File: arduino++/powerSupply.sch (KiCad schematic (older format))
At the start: 10 parts, among them U2 NCP551SN33T1G, U8 LD1085C

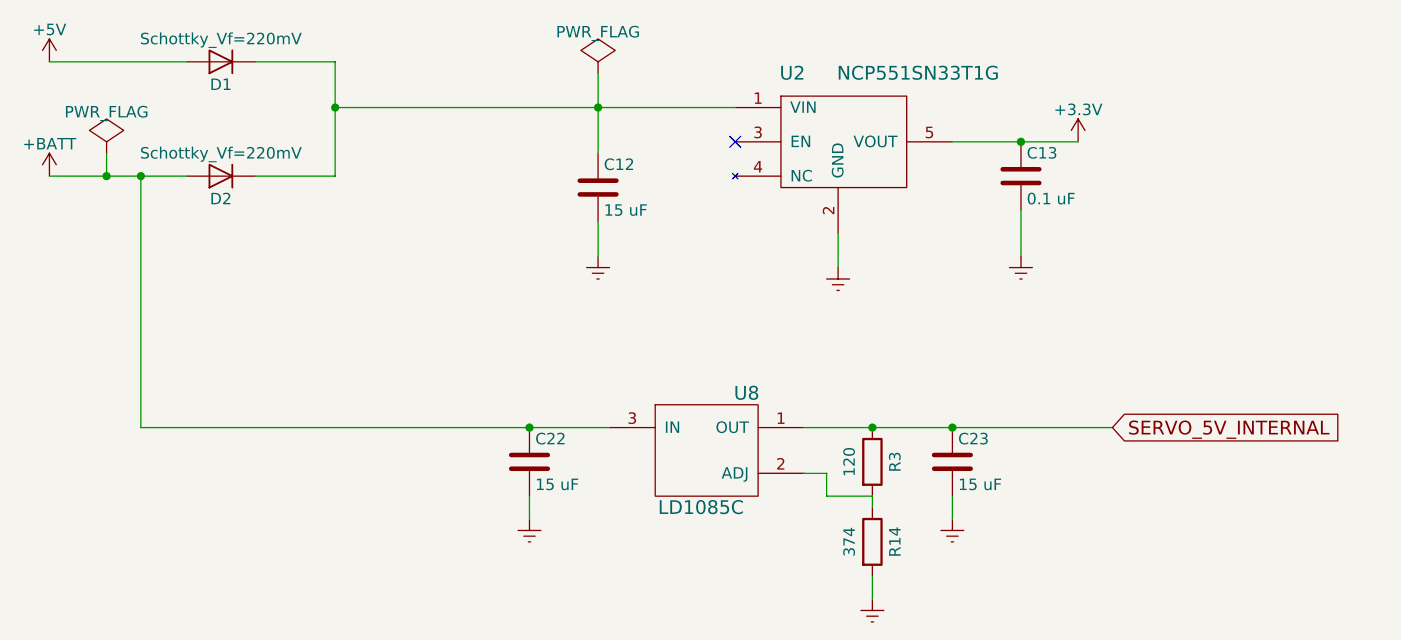
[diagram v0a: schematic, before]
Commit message: Updating to latest rev as ordered on OSHPark.
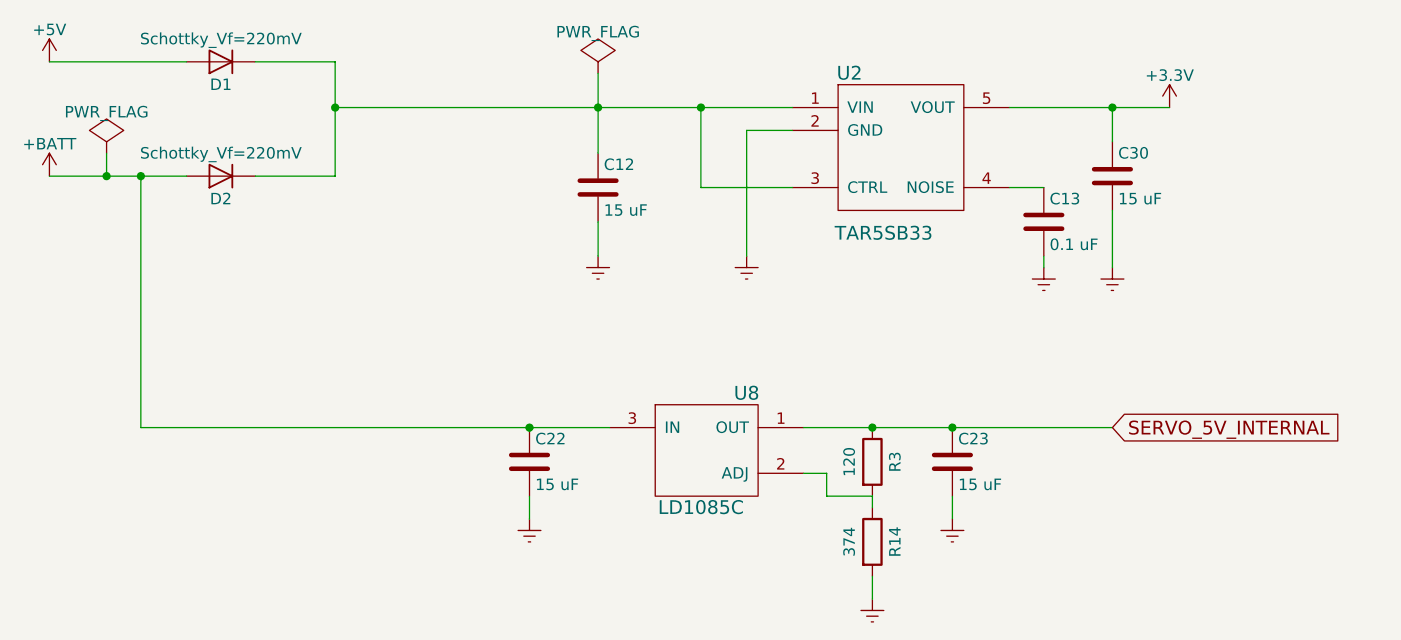
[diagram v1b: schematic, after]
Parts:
- removed U2: NCP551SN33T1G, Housings_SOT-23_SOT-143_TSOT-6:SOT-23-5, symbol NCP551SN33T1G
- added C30: 15 uF, Capacitors_SMD:C_0805_HandSoldering, symbol C
- added U2: TAR5SB33, housings_sot_custom:SC-74A_SOT23-5, symbol TAR5SB33
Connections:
- net +3V3: now also C30.1, U2.5 (VOUT); no longer C13.1
- net Earth: now also C30.2, U2.2 (GND)
- net at C12.1, D1.1 (K), D2.1 (K): now also U2.1 (VIN), U2.3 (CTRL)
- new net: C13.1, U2.4 (NOISE)
- no-connect marks 1 -> 0
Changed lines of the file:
@@
 	4350 3650 4000 3650
 $Comp
-L +5V #PWR054
+L +5V #PWR52
 U 1 1 5834CD49
 P 3100 3150
-F 0 "#PWR054" H 3100 3000 50  0001 C CNN
+F 0 "#PWR52" H 3100 3000 50  0001 C CNN
 F 1 "+5V" H 3100 3290 50  0000 C CNN
 F 2 "" H 3100 3150 50  0000 C CNN
@@
 $EndComp
 Wire Wire Line
-	4350 3350 6100 3350
+	4350 3350 6350 3350
 Connection ~ 4350 3350
 $Comp
-L NCP551SN33T1G U2
-U 1 1 5834E7B3
-P 6600 3500
-F 0 "U2" H 6350 3800 60  0000 C CNN
-F 1 "NCP551SN33T1G" H 6900 3800 60  0000 C CNN
-F 2 "Housings_SOT-23_SOT-143_TSOT-6:SOT-23-5" H 6600 3500 60  0001 C CNN
-F 3 "" H 6600 3500 60  0001 C CNN
-	1    6600 3500
-	1    0    0    -1
-$EndComp
-$Comp
-L Earth #PWR055
+L Earth #PWR56
 U 1 1 5834E86A
-P 6550 4050
-F 0 "#PWR055" H 6550 3800 50  0001 C CNN
-F 1 "Earth" H 6550 3900 50  0001 C CNN
-F 2 "" H 6550 4050 50  0000 C CNN
-F 3 "" H 6550 4050 50  0000 C CNN
-	1    6550 4050
-	1    0    0    -1
-$EndComp
-Wire Wire Line
-	6550 4050 6550 3900
-NoConn ~ 6100 3500
-$Comp
-L +3.3V #PWR056
+P 6150 4000
+F 0 "#PWR56" H 6150 3750 50  0001 C CNN
+F 1 "Earth" H 6150 3850 50  0001 C CNN
+F 2 "" H 6150 4000 50  0000 C CNN
+F 3 "" H 6150 4000 50  0000 C CNN
+	1    6150 4000
+	1    0    0    -1
+$EndComp
+Wire Wire Line
+	6150 3450 6150 4000
+$Comp
+L +3.3V #PWR61
 U 1 1 5834E898
-P 7600 3500
-F 0 "#PWR056" H 7600 3350 50  0001 C CNN
-F 1 "+3.3V" H 7600 3640 50  0000 C CNN
-F 2 "" H 7600 3500 50  0000 C CNN
-F 3 "" H 7600 3500 50  0000 C CNN
-	1    7600 3500
-	1    0    0    -1
-$EndComp
-Wire Wire Line
-	7050 3500 7600 3500
+P 8000 3350
+F 0 "#PWR61" H 8000 3200 50  0001 C CNN
+F 1 "+3.3V" H 8000 3490 50  0000 C CNN
+F 2 "" H 8000 3350 50  0000 C CNN
+F 3 "" H 8000 3350 50  0000 C CNN
+	1    8000 3350
+	1    0    0    -1
+$EndComp
+Wire Wire Line
+	7300 3350 8000 3350
 $Comp
 L C C12
@@
 	1    0    0    -1
 $EndComp
-$Comp
-L C C13
-U 1 1 5834EC33
-P 7350 3650
-F 0 "C13" H 7375 3750 50  0000 L CNN
-F 1 "0.1 uF" H 7375 3550 50  0000 L CNN
-F 2 "Capacitors_SMD:C_0402" H 7388 3500 50  0001 C CNN
-F 3 "" H 7350 3650 50  0000 C CNN
-F 4 "GRM155R61E104KA87D" H 7350 3650 60  0001 C CNN "manf#"
-	1    7350 3650
-	1    0    0    -1
-$EndComp
-Connection ~ 7350 3500
-$Comp
-L Earth #PWR057
+Connection ~ 7750 3350
+$Comp
+L Earth #PWR55
 U 1 1 5834EC66
 P 5500 4000
-F 0 "#PWR057" H 5500 3750 50  0001 C CNN
+F 0 "#PWR55" H 5500 3750 50  0001 C CNN
 F 1 "Earth" H 5500 3850 50  0001 C CNN
 F 2 "" H 5500 4000 50  0000 C CNN
@@
 $EndComp
 $Comp
-L Earth #PWR058
+L Earth #PWR60
 U 1 1 5834EC80
-P 7350 4000
-F 0 "#PWR058" H 7350 3750 50  0001 C CNN
-F 1 "Earth" H 7350 3850 50  0001 C CNN
-F 2 "" H 7350 4000 50  0000 C CNN
-F 3 "" H 7350 4000 50  0000 C CNN
-	1    7350 4000
+P 7750 4050
+F 0 "#PWR60" H 7750 3800 50  0001 C CNN
+F 1 "Earth" H 7750 3900 50  0001 C CNN
+F 2 "" H 7750 4050 50  0000 C CNN
+F 3 "" H 7750 4050 50  0000 C CNN
+	1    7750 4050
 	1    0    0    -1
 $EndComp
@@
 Connection ~ 5500 3350
 Wire Wire Line
-	7350 4000 7350 3800
-$Comp
-L PWR_FLAG #FLG059
+	7750 4050 7750 3800
+$Comp
+L PWR_FLAG #FLG5
 U 1 1 5835C358
 P 5500 3200
-F 0 "#FLG059" H 5500 3295 50  0001 C CNN
+F 0 "#FLG5" H 5500 3295 50  0001 C CNN
 F 1 "PWR_FLAG" H 5500 3380 50  0000 C CNN
 F 2 "" H 5500 3200 50  0000 C CNN
@@
 $EndComp
 $Comp
-L +BATT #PWR060
+L +BATT #PWR53
 U 1 1 58366763
 P 3100 3650
-F 0 "#PWR060" H 3100 3500 50  0001 C CNN
+F 0 "#PWR53" H 3100 3500 50  0001 C CNN
 F 1 "+BATT" H 3100 3790 50  0000 C CNN
 F 2 "" H 3100 3650 50  0000 C CNN
@@
 $EndComp
 $Comp
-L PWR_FLAG #FLG061
+L PWR_FLAG #FLG4
 U 1 1 58366796
 P 3350 3550
-F 0 "#FLG061" H 3350 3645 50  0001 C CNN
+F 0 "#FLG4" H 3350 3645 50  0001 C CNN
 F 1 "PWR_FLAG" H 3350 3730 50  0000 C CNN
 F 2 "" H 3350 3550 50  0000 C CNN
@@
 Connection ~ 5200 4750
 $Comp
-L Earth #PWR062
+L Earth #PWR54
 U 1 1 58A675C7
 P 5200 5150
-F 0 "#PWR062" H 5200 4900 50  0001 C CNN
+F 0 "#PWR54" H 5200 4900 50  0001 C CNN
 F 1 "Earth" H 5200 5000 50  0001 C CNN
 F 2 "" H 5200 5150 50  0000 C CNN
@@
 $EndComp
 $Comp
-L Earth #PWR063
+L Earth #PWR58
 U 1 1 58A675EA
 P 7050 5150
-F 0 "#PWR063" H 7050 4900 50  0001 C CNN
+F 0 "#PWR58" H 7050 4900 50  0001 C CNN
 F 1 "Earth" H 7050 5000 50  0001 C CNN
 F 2 "" H 7050 5150 50  0000 C CNN
@@
 Connection ~ 6700 4750
 $Comp
-L Earth #PWR064
+L Earth #PWR57
 U 1 1 58A67A5B
 P 6700 5500
-F 0 "#PWR064" H 6700 5250 50  0001 C CNN
+F 0 "#PWR57" H 6700 5250 50  0001 C CNN
 F 1 "Earth" H 6700 5350 50  0001 C CNN
 F 2 "" H 6700 5500 50  0000 C CNN
@@
 	-1   0    0    1
 $EndComp
+$Comp
+L TAR5SB33 U2
+U 1 1 58B43669
+P 6800 3550
+F 0 "U2" H 6600 3900 60  0000 C CNN
+F 1 "TAR5SB33" H 6750 3200 60  0000 C CNN
+F 2 "housings_sot_custom:SC-74A_SOT23-5" H 6950 3550 60  0001 C CNN
+F 3 "" H 6950 3550 60  0001 C CNN
+F 4 "TAR5SB33(TE85L,F)" H 6700 4000 60  0001 C CNN "manf#"
+	1    6800 3550
+	1    0    0    -1
+$EndComp
+Wire Wire Line
+	6350 3700 5950 3700
+Wire Wire Line
+	5950 3700 5950 3350
+Connection ~ 5950 3350
+Wire Wire Line
+	6150 3450 6350 3450
+$Comp
+L C C30
+U 1 1 58B43818
+P 7750 3650
+F 0 "C30" H 7775 3750 50  0000 L CNN
+F 1 "15 uF" H 7775 3550 50  0000 L CNN
+F 2 "Capacitors_SMD:C_0805_HandSoldering" H 7788 3500 50  0001 C CNN
+F 3 "" H 7750 3650 50  0000 C CNN
+F 4 "C2012X5R1V156M125AC" H 7750 3650 60  0001 C CNN "manf#"
+	1    7750 3650
+	1    0    0    -1
+$EndComp
+Wire Wire Line
+	7750 3500 7750 3350
+$Comp
+L C C13
+U 1 1 58B43EE4
+P 7450 3850
+F 0 "C13" H 7475 3950 50  0000 L CNN
+F 1 "0.1 uF" H 7475 3750 50  0000 L CNN
+F 2 "Capacitors_SMD:C_0402" H 7488 3700 50  0001 C CNN
+F 3 "" H 7450 3850 50  0000 C CNN
+F 4 "GRM155R61E104KA87D" H 7450 3850 60  0001 C CNN "manf#"
+	1    7450 3850
+	1    0    0    -1
+$EndComp
+Wire Wire Line
+	7300 3700 7450 3700
+$Comp
+L Earth #PWR59
+U 1 1 58B43F91
+P 7450 4050
+F 0 "#PWR59" H 7450 3800 50  0001 C CNN
+F 1 "Earth" H 7450 3900 50  0001 C CNN
+F 2 "" H 7450 4050 50  0000 C CNN
+F 3 "" H 7450 4050 50  0000 C CNN
+	1    7450 4050
+	1    0    0    -1
+$EndComp
+Wire Wire Line
+	7450 4050 7450 4000
 $EndSCHEMATC
